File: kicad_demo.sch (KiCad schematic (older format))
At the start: 15 parts, among them P1 pwr, P2 key, Q1 2N3053, Y1 7020 kHz

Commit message: Make schematic + part selection more real-world friendly
Hand-wound air coils w/ custom footprint
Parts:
- removed C2: 1000pF, Potentiometers:Potentiometer_Bourns_3339H_Angular_ScrewUp, symbol C_Variable
- removed C5: 267pF, Capacitors_SMD:C_1206_HandSoldering, symbol C
- removed Q1: 2N3053, TO_SOT_Packages_THT:TO39EBC, symbol Q_NPN_BCE
- added C10, C13, C7: 60p, Resistors_Universal:Resistor_SMD+THTuniversal_0805to1206_RM10_HandSoldering, symbol C
- added C11: 5p, Resistors_Universal:Resistor_SMD+THTuniversal_0805to1206_RM10_HandSoldering, symbol C
- added C12, C6: 200p, Resistors_Universal:Resistor_SMD+THTuniversal_0805to1206_RM10_HandSoldering, symbol C
- added C14, C8: 7p, Resistors_Universal:Resistor_SMD+THTuniversal_0805to1206_RM10_HandSoldering, symbol C
- added C3: 100p, Resistors_Universal:Resistor_SMD+THTuniversal_0805to1206_RM10_HandSoldering, symbol C
- added C9: 800p, Resistors_Universal:Resistor_SMD+THTuniversal_0805to1206_RM10_HandSoldering, symbol C
- added Q1: BC546, TO_SOT_Packages_THT:TO-92_Molded_Wide, symbol Q_NPN_CBE
- added R2: 0, Resistors_Universal:Resistor_SMD+THTuniversal_0805to1206_RM10_HandSoldering, symbol R
- C1: footprint Capacitors_SMD:C_1206_HandSoldering -> Resistors_Universal:Resistor_SMD+THTuniversal_0805to1206_RM10_HandSoldering
- C2: renamed from C6; footprint Capacitors_SMD:C_1206_HandSoldering -> Resistors_Universal:Resistor_SMD+THTuniversal_0805to1206_RM10_HandSoldering
- C4: value 865pF -> 100p; footprint Capacitors_SMD:C_1206_HandSoldering -> Resistors_Universal:Resistor_SMD+THTuniversal_0805to1206_RM10_HandSoldering
- C5: renamed from C3; value 267pF -> 100p; footprint Capacitors_SMD:C_1206_HandSoldering -> Resistors_Universal:Resistor_SMD+THTuniversal_0805to1206_RM10_HandSoldering
- L2, L3: footprint Inductors:Inductor_Vishay_IHSM-3825 -> PROJECT:1u75_coil
- P2: footprint Buttons_Switches_ThroughHole:SW_PUSH -> Buttons_Switches_ThroughHole:SW_PUSH_6mm
- R1: footprint Resistors_ThroughHole:Resistor_Horizontal_RM15mm -> Resistors_Universal:Resistor_SMD+THTuniversal_0805to1206_RM10_HandSoldering
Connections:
- wire segments 32 -> 54
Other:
- note added: "1000p trimmer originally"
- note added: "Coils are 24 turns of 1.5 mm insulated wire on 10 mm former\nhttp://mustcalculate.com/electronics/singlelayeraircoil.php?d=11.5&du=mm&l=36&lu=mm&i=1.75u"
- note added: "Optional filter bypass"
- moved on the sheet: AE1, C5, L2, L3

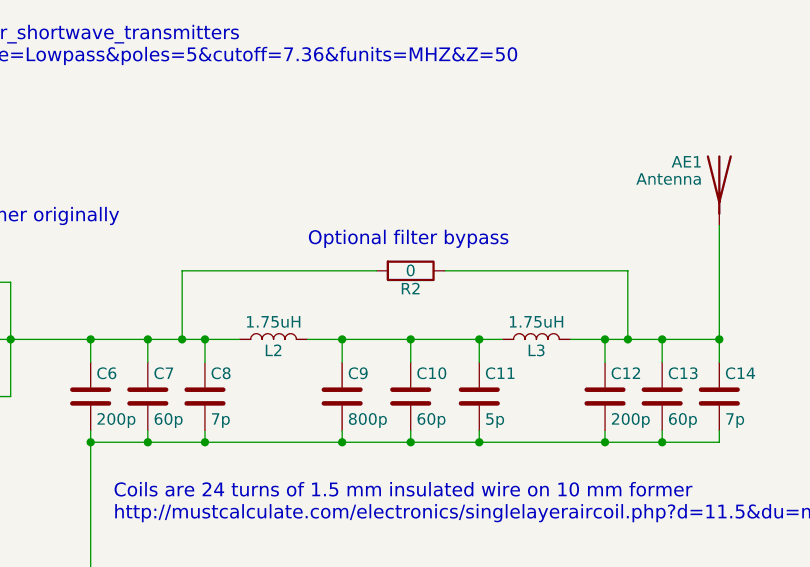
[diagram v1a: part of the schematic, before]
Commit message: Rough layout
Want to route signal and GND on top to minimize current loop size
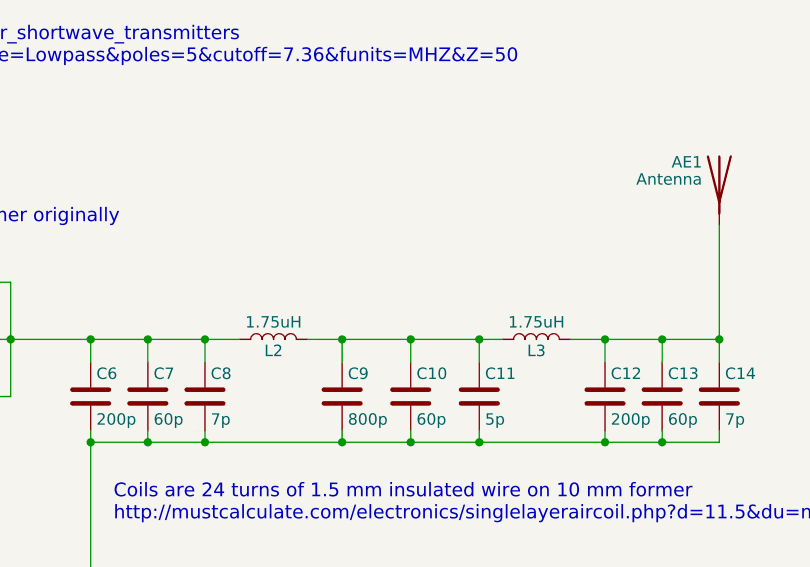
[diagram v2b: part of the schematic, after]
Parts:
- removed R2: 0, Resistors_Universal:Resistor_SMD+THTuniversal_0805to1206_RM10_HandSoldering, symbol R
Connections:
- wire segments 54 -> 50
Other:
- note removed: "Optional filter bypass"
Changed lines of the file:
@@
 Text Notes 4700 2200 0    60   ~ 0
 1000p trimmer originally
-$Comp
-L R R2
-U 1 1 5AA9AA3F
-P 7000 2400
-F 0 "R2" V 7080 2400 50  0000 C CNN
-F 1 "0" V 7000 2400 50  0000 C CNN
-F 2 "Resistors_Universal:Resistor_SMD+THTuniversal_0805to1206_RM10_HandSoldering" V 6930 2400 50  0001 C CNN
-F 3 "" H 7000 2400 50  0000 C CNN
-	1    7000 2400
-	0    1    1    0
-$EndComp
-Wire Wire Line
-	7150 2400 7950 2400
-Wire Wire Line
-	7950 2400 7950 2700
-Connection ~ 7950 2700
-Wire Wire Line
-	6850 2400 6000 2400
-Wire Wire Line
-	6000 2400 6000 2700
-Connection ~ 6000 2700
-Text Notes 6550 2300 0    60   ~ 0
-Optional filter bypass
 Text Notes 5700 3500 0    60   ~ 0
 Coils are 24 turns of 1.5 mm insulated wire on 10 mm former\nhttp://mustcalculate.com/electronics/singlelayeraircoil.php?d=11.5&du=mm&l=36&lu=mm&i=1.75u

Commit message: Fiddle with layout, add more transistors
Vertically centered L2 wrt L3, to reduce coupling.
Increased distance between signal and GND trace.
Added two copies of Q1 next to it, in case more power is wanted.
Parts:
- added Q2, Q3: BC546, TO_SOT_Packages_THT:TO-92_Molded_Wide, symbol Q_NPN_CBE
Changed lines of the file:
@@
 U 1 1 5AA980E8
 P 4300 3050
-F 0 "Q1" H 4500 3100 50  0000 L CNN
+F 0 "Q1" H 4500 3300 50  0000 L CNN
 F 1 "BC546" H 4500 3000 50  0000 L CNN
 F 2 "TO_SOT_Packages_THT:TO-92_Molded_Wide" H 4500 3150 50  0001 C CNN
@@
 Text Notes 5700 3500 0    60   ~ 0
 Coils are 24 turns of 1.5 mm insulated wire on 10 mm former\nhttp://mustcalculate.com/electronics/singlelayeraircoil.php?d=11.5&du=mm&l=36&lu=mm&i=1.75u
+$Comp
+L Q_NPN_CBE Q2
+U 1 1 5AAAB82A
+P 4300 3050
+F 0 "Q2" H 4500 3200 50  0000 L CNN
+F 1 "BC546" H 4500 3000 50  0000 L CNN
+F 2 "TO_SOT_Packages_THT:TO-92_Molded_Wide" H 4500 3150 50  0001 C CNN
+F 3 "" H 4300 3050 50  0000 C CNN
+	1    4300 3050
+	1    0    0    -1
+$EndComp
+$Comp
+L Q_NPN_CBE Q3
+U 1 1 5AAABC4C
+P 4300 3050
+F 0 "Q3" H 4500 3100 50  0000 L CNN
+F 1 "BC546" H 4500 3000 50  0000 L CNN
+F 2 "TO_SOT_Packages_THT:TO-92_Molded_Wide" H 4500 3150 50  0001 C CNN
+F 3 "" H 4300 3050 50  0000 C CNN
+	1    4300 3050
+	1    0    0    -1
+$EndComp
 $EndSCHEMATC

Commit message: Add test points, winding instruction on F.SilkS
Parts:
- added W1, W2, W3, W4, W5, W6: TEST_1P, Pin_Headers:Pin_Header_Straight_1x01, symbol TEST_1P
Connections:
- wire segments 50 -> 52
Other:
- moved on the sheet: L1
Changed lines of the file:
@@
 L L_Core_Ferrite L1
 U 1 1 5A6A33ED
-P 4400 2300
-F 0 "L1" V 4350 2300 50  0000 C CNN
-F 1 "100uH" V 4510 2300 50  0000 C CNN
-F 2 "Choke_Axial_ThroughHole:Choke_Horizontal_RM20mm" H 4400 2300 50  0001 C CNN
-F 3 "" H 4400 2300 50  0000 C CNN
-	1    4400 2300
+P 4400 2250
+F 0 "L1" V 4350 2250 50  0000 C CNN
+F 1 "100uH" V 4510 2250 50  0000 C CNN
+F 2 "Choke_Axial_ThroughHole:Choke_Horizontal_RM20mm" H 4400 2250 50  0001 C CNN
+F 3 "" H 4400 2250 50  0000 C CNN
+	1    4400 2250
 	1    0    0    -1
 $EndComp
@@
 	3400 2050 4400 2050
 Wire Wire Line
-	4400 2050 4400 2150
+	4400 2050 4400 2100
 Connection ~ 3950 3750
 Wire Wire Line
@@
 Connection ~ 4400 2650
 Wire Wire Line
-	4400 2450 4400 2850
+	4400 2400 4400 2850
 Wire Wire Line
 	4250 2650 4400 2650
@@
 	3900 2650 3950 2650
 Wire Wire Line
-	3900 3050 3900 2650
+	3900 2600 3900 3050
 Wire Wire Line
 	3800 3050 4100 3050
@@
 	4400 3350 4400 3250
 Wire Wire Line
-	4250 3350 4500 3350
+	4200 3350 4500 3350
 Wire Wire Line
 	4250 3400 4250 3350
@@
 Connection ~ 7300 2700
 Wire Wire Line
-	7000 2800 7000 2700
+	7000 2650 7000 2800
 Connection ~ 7000 2700
 Wire Wire Line
@@
 Connection ~ 8350 2700
 Wire Wire Line
-	8100 2700 8100 2800
+	8100 2650 8100 2800
 Connection ~ 8100 2700
 Wire Wire Line
@@
 	1    0    0    -1
 $EndComp
+$Comp
+L TEST_1P W1
+U 1 1 5AAC07A8
+P 4600 2650
+F 0 "W1" H 4600 2850 50  0000 C CNN
+F 1 "TEST_1P" H 4600 2850 50  0001 C CNN
+F 2 "Pin_Headers:Pin_Header_Straight_1x01" H 4800 2650 50  0001 C CNN
+F 3 "" H 4800 2650 50  0000 C CNN
+	1    4600 2650
+	1    0    0    -1
+$EndComp
+Wire Wire Line
+	4600 2650 4600 2700
+Connection ~ 4600 2700
+$Comp
+L TEST_1P W2
+U 1 1 5AAC0B76
+P 3900 2600
+F 0 "W2" H 3900 2800 50  0000 C CNN
+F 1 "TEST_1P" H 3900 2800 50  0001 C CNN
+F 2 "Pin_Headers:Pin_Header_Straight_1x01" H 4100 2600 50  0001 C CNN
+F 3 "" H 4100 2600 50  0000 C CNN
+	1    3900 2600
+	1    0    0    -1
+$EndComp
+Connection ~ 3900 2650
+$Comp
+L TEST_1P W3
+U 1 1 5AAC0FB3
+P 5450 2650
+F 0 "W3" H 5450 2850 50  0000 C CNN
+F 1 "TEST_1P" H 5450 2850 50  0001 C CNN
+F 2 "Pin_Headers:Pin_Header_Straight_1x01" H 5650 2650 50  0001 C CNN
+F 3 "" H 5650 2650 50  0000 C CNN
+	1    5450 2650
+	1    0    0    -1
+$EndComp
+Wire Wire Line
+	5450 2700 5450 2650
+Connection ~ 5450 2700
+$Comp
+L TEST_1P W4
+U 1 1 5AAC1158
+P 7000 2650
+F 0 "W4" H 7000 2850 50  0000 C CNN
+F 1 "TEST_1P" H 7000 2850 50  0001 C CNN
+F 2 "Pin_Headers:Pin_Header_Straight_1x01" H 7200 2650 50  0001 C CNN
+F 3 "" H 7200 2650 50  0000 C CNN
+	1    7000 2650
+	1    0    0    -1
+$EndComp
+$Comp
+L TEST_1P W5
+U 1 1 5AAC1388
+P 8100 2650
+F 0 "W5" H 8100 2850 50  0000 C CNN
+F 1 "TEST_1P" H 8100 2850 50  0001 C CNN
+F 2 "Pin_Headers:Pin_Header_Straight_1x01" H 8300 2650 50  0001 C CNN
+F 3 "" H 8300 2650 50  0000 C CNN
+	1    8100 2650
+	1    0    0    -1
+$EndComp
+$Comp
+L TEST_1P W6
+U 1 1 5AAC16F8
+P 4200 3350
+F 0 "W6" H 4200 3550 50  0000 C CNN
+F 1 "TEST_1P" H 4200 3550 50  0001 C CNN
+F 2 "Pin_Headers:Pin_Header_Straight_1x01" H 4400 3350 50  0001 C CNN
+F 3 "" H 4400 3350 50  0000 C CNN
+	1    4200 3350
+	0    -1   -1   0
+$EndComp
+Connection ~ 4250 3350
 $EndSCHEMATC

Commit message: License under TAPR Open Hardware License Version 1.0
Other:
- note added: "Licensed under the TAPR Open Hardware License Version 1.0"
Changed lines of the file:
@@
 $EndComp
 Connection ~ 4250 3350
+Text Notes 2950 850  0    60   ~ 0
+Licensed under the TAPR Open Hardware License Version 1.0
 $EndSCHEMATC

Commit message: Add some useful power test points
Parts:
- added W10, W7, W8, W9: TEST_1P, Pin_Headers:Pin_Header_Straight_1x01, symbol TEST_1P
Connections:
- wire segments 52 -> 56
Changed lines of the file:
@@
 Text Notes 2950 850  0    60   ~ 0
 Licensed under the TAPR Open Hardware License Version 1.0
+$Comp
+L TEST_1P W7
+U 1 1 5AAED88E
+P 4150 2000
+F 0 "W7" H 4150 2200 50  0000 C CNN
+F 1 "TEST_1P" H 4150 2200 50  0001 C CNN
+F 2 "Pin_Headers:Pin_Header_Straight_1x01" H 4350 2000 50  0001 C CNN
+F 3 "" H 4350 2000 50  0000 C CNN
+	1    4150 2000
+	1    0    0    -1
+$EndComp
+$Comp
+L TEST_1P W8
+U 1 1 5AAED942
+P 4300 2000
+F 0 "W8" H 4300 2200 50  0000 C CNN
+F 1 "TEST_1P" H 4300 2200 50  0001 C CNN
+F 2 "Pin_Headers:Pin_Header_Straight_1x01" H 4500 2000 50  0001 C CNN
+F 3 "" H 4500 2000 50  0000 C CNN
+	1    4300 2000
+	1    0    0    -1
+$EndComp
+Wire Wire Line
+	4150 2000 4150 2050
+Connection ~ 4150 2050
+Wire Wire Line
+	4300 2000 4300 2050
+Connection ~ 4300 2050
+$Comp
+L TEST_1P W9
+U 1 1 5AAEDAD1
+P 5000 3700
+F 0 "W9" H 5000 3900 50  0000 C CNN
+F 1 "TEST_1P" H 5000 3900 50  0001 C CNN
+F 2 "Pin_Headers:Pin_Header_Straight_1x01" H 5200 3700 50  0001 C CNN
+F 3 "" H 5200 3700 50  0000 C CNN
+	1    5000 3700
+	1    0    0    -1
+$EndComp
+$Comp
+L TEST_1P W10
+U 1 1 5AAEDB8B
+P 5150 3700
+F 0 "W10" H 5150 3900 50  0000 C CNN
+F 1 "TEST_1P" H 5150 3900 50  0001 C CNN
+F 2 "Pin_Headers:Pin_Header_Straight_1x01" H 5350 3700 50  0001 C CNN
+F 3 "" H 5350 3700 50  0000 C CNN
+	1    5150 3700
+	1    0    0    -1
+$EndComp
+Wire Wire Line
+	5000 3700 5000 3750
+Connection ~ 5000 3750
+Wire Wire Line
+	5150 3700 5150 3750
+Connection ~ 5150 3750
 $EndSCHEMATC

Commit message: Final version, hopefully
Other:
- note added: "1000p trimmer originally\n100 pF works well\nSomewhere between 100-220 pF was the sweet spot, power-wise\nApprox 60 mW into 50 Ohm load from 9V supply"
- note removed: "1000p trimmer originally"
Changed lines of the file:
@@
 Connection ~ 8100 3150
 Text Notes 4700 2200 0    60   ~ 0
-1000p trimmer originally
+1000p trimmer originally\n100 pF works well\nSomewhere between 100-220 pF was the sweet spot, power-wise\nApprox 60 mW into 50 Ohm load from 9V supply
 Text Notes 5700 3500 0    60   ~ 0
 Coils are 24 turns of 1.5 mm insulated wire on 10 mm former\nhttp://mustcalculate.com/electronics/singlelayeraircoil.php?d=11.5&du=mm&l=36&lu=mm&i=1.75u

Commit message: Mouser BOM
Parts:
- AE1, C11, L2, L3, W1, W10, W2, W3, W4, W5, W6, W7, W8, W9: fit_field (none) -> dnf
- C1, C2: Mfg. Name (none) -> Panasonic; Mfg. Part Number (none) -> ECH-U1H103JX5; Mouser PN (none) -> 667-ECH-U1H103JX5
- C10: value 60p -> 40p; fit_field (none) -> dnf
- C12, C6: value 200p -> 270p; Mfg. Name (none) -> TDK; Mfg. Part Number (none) -> FG28C0G1H271JNT00; Mouser PN (none) -> 810-FG28C0G1H271JNT0
- C13, C7: value 60p -> 0p; fit_field (none) -> dnf
- C14, C8: value 7p -> 0p; fit_field (none) -> dnf
- C3: Mfg. Name (none) -> TDK; Mfg. Part Number (none) -> FA28C0G1H101JNU00; Mouser PN (none) -> 810-FA28C0G1H10100
- C4, C5: value 100p -> 0p; fit_field (none) -> dnf
- C9: value 800p -> 820p; Mfg. Name (none) -> TDK; Mfg. Part Number (none) -> FG28C0G1H821JNT00; Mouser PN (none) -> 810-FG28C0G1H821JNT0
- L1: Mfg. Name (none) -> Bourns; Mfg. Part Number (none) -> 78F101J-RC; Mouser PN (none) -> 542-78F101-RC
- P1: Mfg. Name (none) -> Keystone Electronics; Mfg. Part Number (none) -> 81-8; Mouser PN (none) -> 534-81-8TB
- P2: Mfg. Name (none) -> TE Connectivity; Mfg. Part Number (none) -> FSM2JLH; Mouser PN (none) -> 506-FSM2JLH
- Q1: Mfg. Name (none) -> Taiwan Semiconductor; Mfg. Part Number (none) -> BC546B A1; Mouser PN (none) -> 821-BC546B-A1
- Q2, Q3: Mfg. Name (none) -> Taiwan Semiconductor; Mfg. Part Number (none) -> BC546B A1; Mouser PN (none) -> 821-BC546B-A1; fit_field (none) -> dnf
- R1: Mfg. Name (none) -> Bourns; Mfg. Part Number (none) -> CR1206-FX-2202ELF; Mouser PN (none) -> 652-CR1206FX-2202ELF
- Y1: value 7020 kHz -> 7030 kHz; Mfg. Name (none) -> IQD; Mfg. Part Number (none) -> LFXTAL011525Bulk; Mouser PN (none) -> 449-LFXTAL011525BULK
